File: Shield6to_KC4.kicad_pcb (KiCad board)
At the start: 2 copper layers, 23 parts, among them J1 DB9, P1 CONN_8, P2 CONN_8, P3 CONN_9, P4 CONN_9, P5 CONN_8, P6 CONN_8, P7 CONN_8, P8 CONN_8, U1 ID-12LA, U2 MAX232

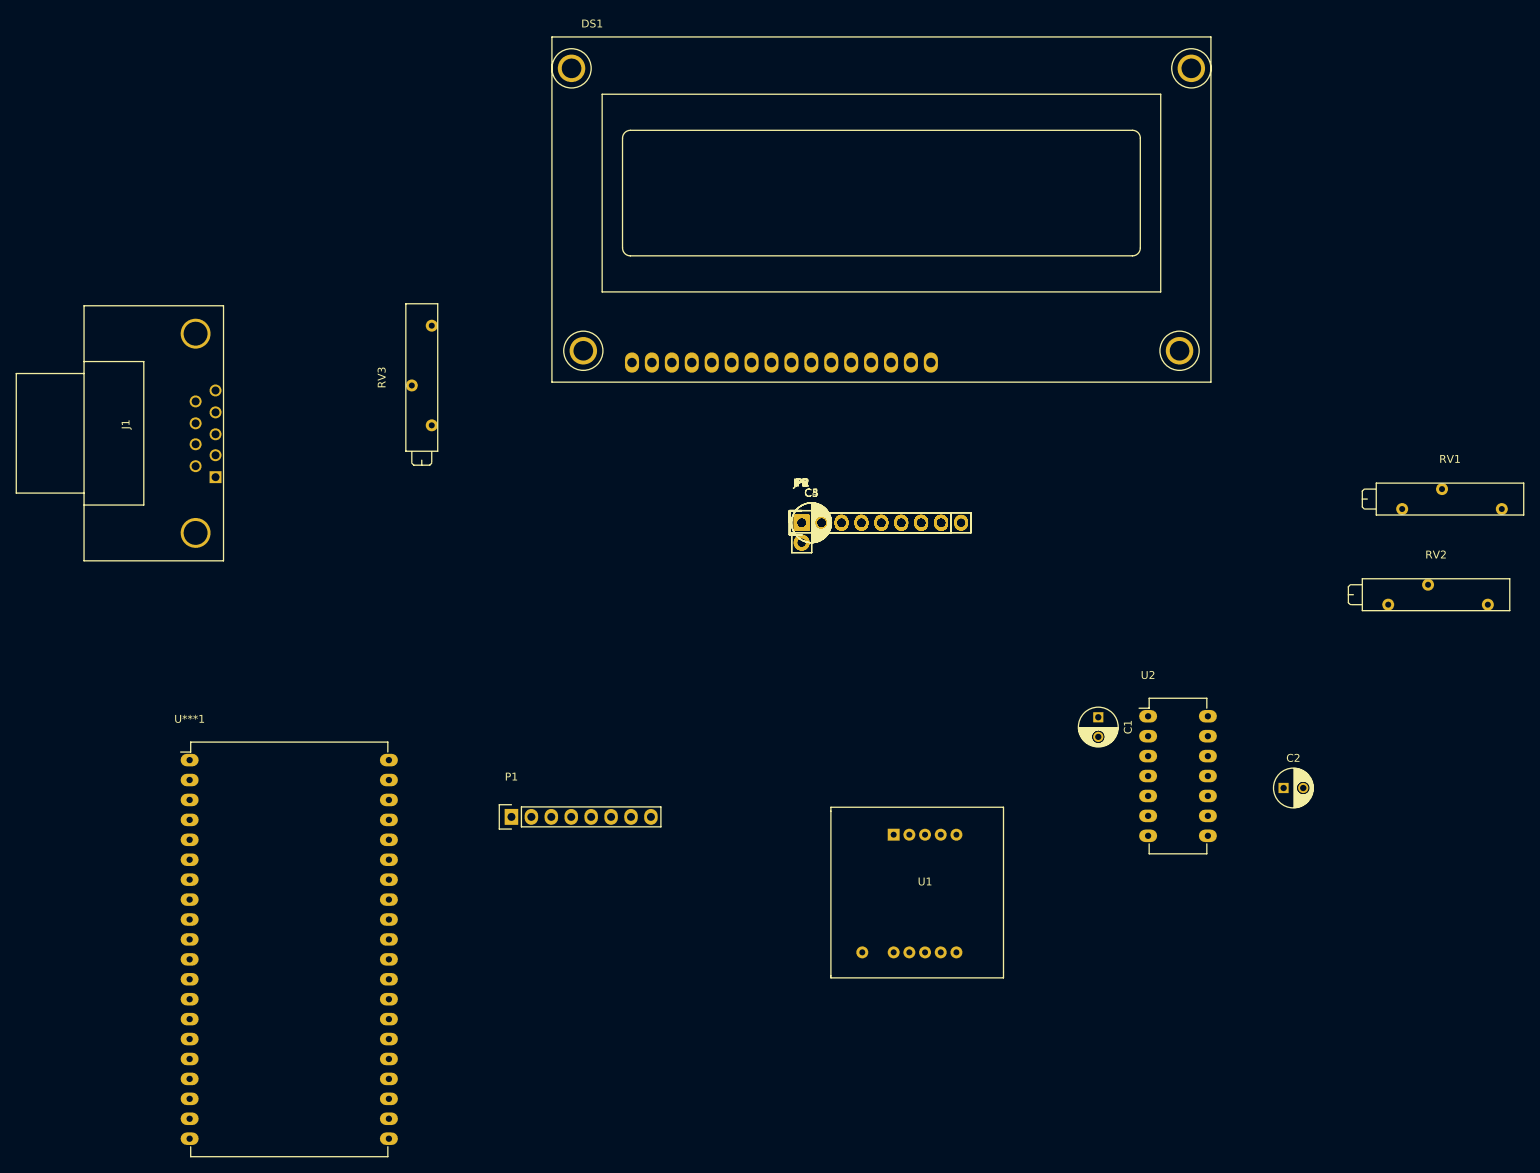
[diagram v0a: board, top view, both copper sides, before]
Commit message: Changes to be committed: 	deleted:    Shield6to-cache.lib 	deleted:    Shield6to-rescue.lib 	deleted:    Shield6to.cmp 	deleted:    Shield6to.net 	modified:   Shield6to_KC4-cache.lib 	renamed:    Shield6to.sch -> Shield6to_KC4.bak 	modified:   Shield6to_KC4.kicad_pcb 	modified:   Shield6to_KC4.kicad_pcb-bak 	modified:   Shield6to_KC4.net 	modified:   Shield6to_KC4.sch
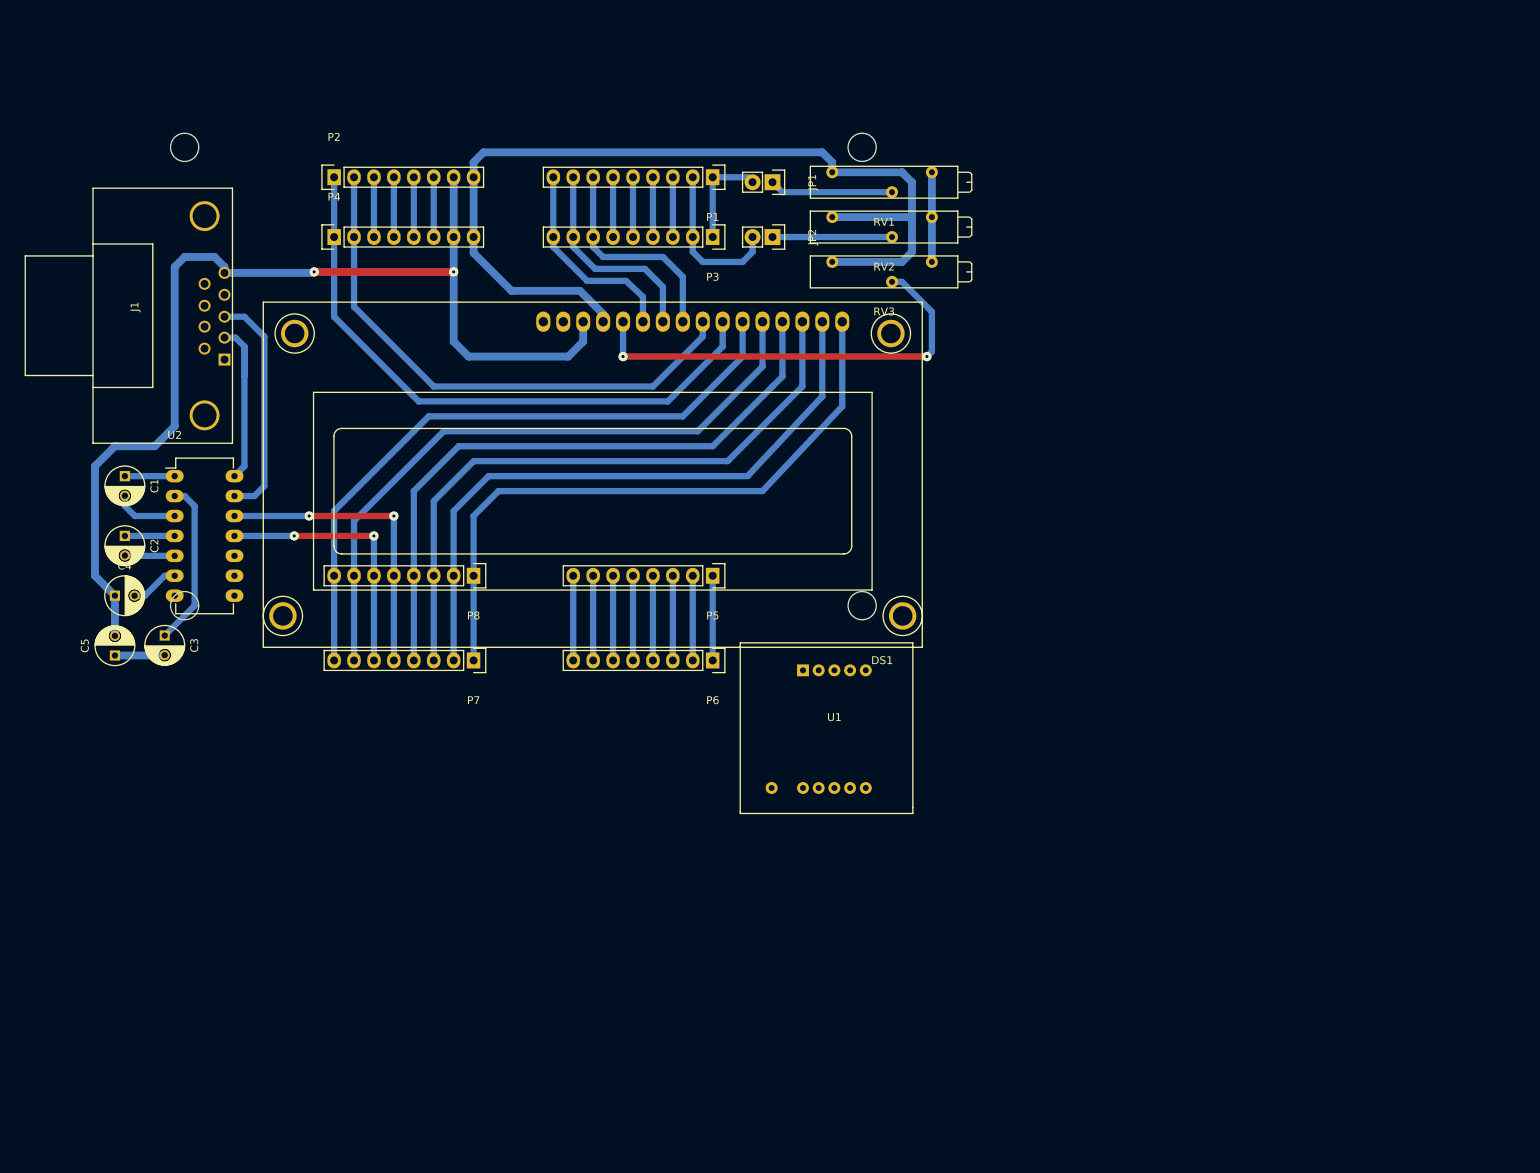
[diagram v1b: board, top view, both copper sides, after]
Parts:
- removed U***1: PIC18F4550, Housings_DIP:DIP-40_W25.4mm_LongPads
- C3: value 10uF -> 1uF
- C5: value 1uF -> 10uF
- P1: value CONN_8 -> CONN_9; footprint Socket_Strips:Socket_Strip_Straight_1x08 -> Socket_Strips:Socket_Strip_Straight_1x09
- P4: value CONN_9 -> CONN_8; footprint Socket_Strips:Socket_Strip_Straight_1x09 -> Socket_Strips:Socket_Strip_Straight_1x08
- moved C2 151.2 mm to (62.2, 106.7), turned to 270 degrees
- moved C1 127.8 mm to (62.2, 99.1)
- moved U2 127.8 mm to (68.6, 99.1)
- moved RV2 97.1 mm to (152.4, 66.0), turned to 180 degrees
- moved RV1 95.5 mm to (152.4, 60.3), turned to 180 degrees
- moved C5 89.2 mm to (61.0, 121.9), turned to 90 degrees
- moved C4 88.0 mm to (61.0, 114.3)
- moved P1 85.5 mm to (137.2, 61.0), turned to 180 degrees
- moved C3 82.5 mm to (67.3, 119.4), turned to 270 degrees
- moved P2 74.1 mm to (88.9, 61.0)
- moved P4 69.8 mm to (88.9, 68.6)
- moved RV3 51.7 mm to (152.4, 71.8), turned to 180 degrees
- moved P7 45.4 mm to (106.7, 122.6), turned to 180 degrees
- moved JP1 43.6 mm to (144.8, 61.6), turned to 270 degrees
- moved P8 42.4 mm to (106.7, 111.8), turned to 180 degrees
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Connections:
- net Net-(P5-Pad3) renamed /RB5
- net Net-(P5-Pad4) renamed /RB4
- net Net-(P5-Pad5) renamed /RB3
- net Net-(P5-Pad6) renamed /RB2
- C2 pad 2: +5V -> Net-(C2-Pad2)
- C3 pad 1: +5V -> Net-(C3-Pad1)
- C3 pad 2: GND -> +5V
- C4 pad 1: Net-(C4-Pad1) -> GND
- C5 pad 1: GND -> +5V
- C5 pad 2: Net-(C5-Pad2) -> GND
- JP1 pad 2: Net-(JP1-Pad2) -> /RA0
- JP2 pad 2: Net-(JP2-Pad2) -> /RA1
- P1 pad 1: Net-(P1-Pad1) -> /RA0
- P1 pad 2: Net-(P1-Pad2) -> /RA1
- P1 pad 3: Net-(P1-Pad3) -> /RA2
- P1 pad 4: Net-(P1-Pad4) -> /RA3
- P1 pad 5: Net-(P1-Pad5) -> /RA4
- P1 pad 6: Net-(P1-Pad6) -> /RA5
- P1 pad 7: Net-(P1-Pad7) -> En
- P1 pad 8: Net-(P1-Pad8) -> R/W
- P2 pad 1: Net-(P1-Pad1) -> /RD1
- P2 pad 2: Net-(P1-Pad2) -> /RD0
- P2 pad 3: Net-(P1-Pad3) -> /RE3
- P2 pad 4: Net-(P1-Pad4) -> /RC2
- P2 pad 5: Net-(P1-Pad5) -> /RC1
- P2 pad 6: Net-(P1-Pad6) -> /RC0
- P2 pad 7: Net-(P1-Pad7) -> GND
- P2 pad 8: Net-(P1-Pad8) -> +5V
- P3 pad 1: Net-(JP1-Pad2) -> /RA0
- P3 pad 2: Net-(JP2-Pad2) -> /RA1
- P3 pad 3: Net-(P3-Pad3) -> /RA2
- P3 pad 4: Net-(P3-Pad4) -> /RA3
- P3 pad 5: Net-(P3-Pad5) -> /RA4
- P3 pad 6: Net-(P3-Pad6) -> /RA5
- P4 pad 1: Net-(JP1-Pad2) -> /RD1
- P4 pad 2: Net-(JP2-Pad2) -> /RD0
- P4 pad 3: Net-(P3-Pad3) -> /RE3
- P4 pad 4: Net-(P3-Pad4) -> /RC2
- P4 pad 5: Net-(P3-Pad5) -> /RC1
- P4 pad 6: Net-(P3-Pad6) -> /RC0
- P4 pad 7: En -> GND
- P4 pad 8: R/W -> +5V
- P5 pad 1: /RD1 -> /RB7
- P5 pad 2: /RD0 -> /RB6
- P5 pad 7: GND -> /RB1
- P5 pad 8: +5V -> /RB0
- P6 pad 1: /RD1 -> /RB7
- P6 pad 2: /RD0 -> /RB6
- P6 pad 7: GND -> /RB1
- P6 pad 8: +5V -> /RB0
- P7 pad 5: Net-(P7-Pad5) -> RX
- P7 pad 6: Net-(P7-Pad6) -> TX
- U2 pad 2: Net-(C2-Pad1) -> Net-(C3-Pad1)
- U2 pad 4: Net-(C4-Pad1) -> Net-(C2-Pad1)
- U2 pad 5: Net-(C4-Pad2) -> Net-(C2-Pad2)
- U2 pad 6: Net-(C5-Pad2) -> Net-(C4-Pad2)
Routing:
- net GND: track 0.00 -> 146.3 mm, vias 0 -> 2
- net +5V: track 0.00 -> 127.1 mm
- net /RD3: track 0.00 -> 83.7 mm
- net /RD2: track 0.00 -> 83.7 mm
- net /RD7: track 0.00 -> 82.2 mm
- net /RD6: track 0.00 -> 81.8 mm
- net /RD5: track 0.00 -> 81.6 mm
- net /RD4: track 0.00 -> 81.6 mm
- net /RD1: track 0.00 -> 77.8 mm
- net /RD0: track 0.00 -> 69.7 mm
- net Net-(DS1-Pad3): track 0.00 -> 55.8 mm, vias 0 -> 2
- net RX: track 0.00 -> 39.4 mm, vias 0 -> 2
- net TX: track 0.00 -> 33.7 mm, vias 0 -> 2
- net Net-(J1-Pad3): track 0.00 -> 29.5 mm
- net En: track 0.00 -> 27.6 mm
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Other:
- board outline added: 90 x 62 mm
- net class Default: trace_width 0.25 -> 0.8; via_dia 0.6 -> 1.2
- net class Power added: clearance 0.2, trace_width 1, via_dia 1.2, via_drill 0.4

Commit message: Primera version de la Placa lista para la Revision de MArtín
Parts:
- removed U1: ID-12LA, Librerias:ID12-LA
- U2: footprint Housings_DIP:DIP-14_W7.62mm_LongPads -> Housings_DIP:DIP-16_W7.62mm
- moved P5 10.2 mm to (137.2, 101.6)
- moved P8 10.2 mm to (106.7, 101.6)
- moved C3 5.08 mm to (72.4, 119.4)
- moved C4 4.96 mm to (64.8, 111.1), turned to 90 degrees
- moved C1 4.58 mm to (64.8, 95.2)
- moved C2 4.58 mm to (64.8, 102.9)
- moved U2 4.02 mm to (69.8, 95.2)
- moved C5 3.81 mm to (64.8, 121.9)
- moved P3 3.17 mm to (137.2, 65.4)
- moved P4 3.17 mm to (88.9, 65.4)
- moved J1 2.54 mm to (73.7, 76.2)
- moved DS1 0.64 mm to (120.7, 78.7)
- moved JP1 0.63 mm to (144.8, 61.0)
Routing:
- net GND: track 146.3 -> 363.0 mm, vias 2 -> 0
- net +5V: track 127.1 -> 218.9 mm, vias 0 -> 6
- net TX: track 33.7 -> 57.6 mm
- net Net-(DS1-Pad3): track 55.8 -> 39.3 mm
- net RX: track 39.4 -> 52.2 mm
- net /RB7: track 10.8 -> 21.0 mm
- net /RB6: track 10.8 -> 21.0 mm
- net /RB5: track 10.8 -> 21.0 mm
- net /RB4: track 10.8 -> 21.0 mm
- net /RB3: track 10.8 -> 21.0 mm
- net /RB2: track 10.8 -> 21.0 mm
- net /RB1: track 10.8 -> 21.0 mm
- net /RB0: track 10.8 -> 21.0 mm
- net /RD1: track 77.8 -> 68.7 mm
- net /RD0: track 69.7 -> 60.9 mm
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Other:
- board size 90 x 62 mm -> 109.2 x 80 mm
